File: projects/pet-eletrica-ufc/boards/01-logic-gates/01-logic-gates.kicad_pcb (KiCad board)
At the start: 2 copper layers, 114 x 144 mm, 18 parts, among them J1 5V INPUT, SW1 B3F-4050, SW2 B3F-4050, U1 SN74HC08N, U2 SN74HC32N, U3 SN74HC04N

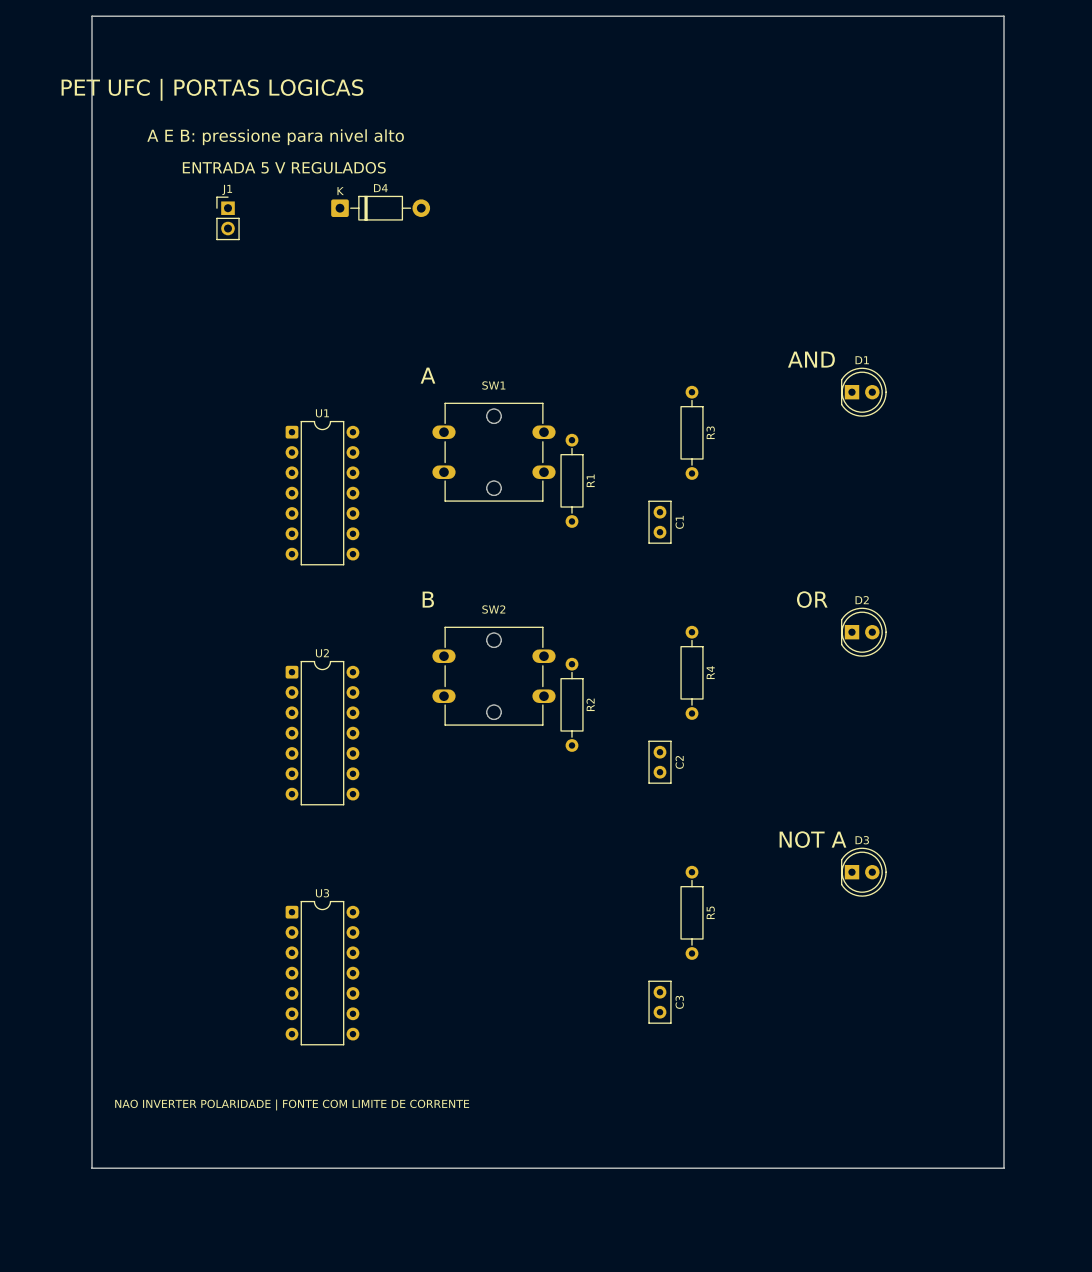
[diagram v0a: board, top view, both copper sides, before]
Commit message: feat(pet-ufc): implement discrete transistor logic board
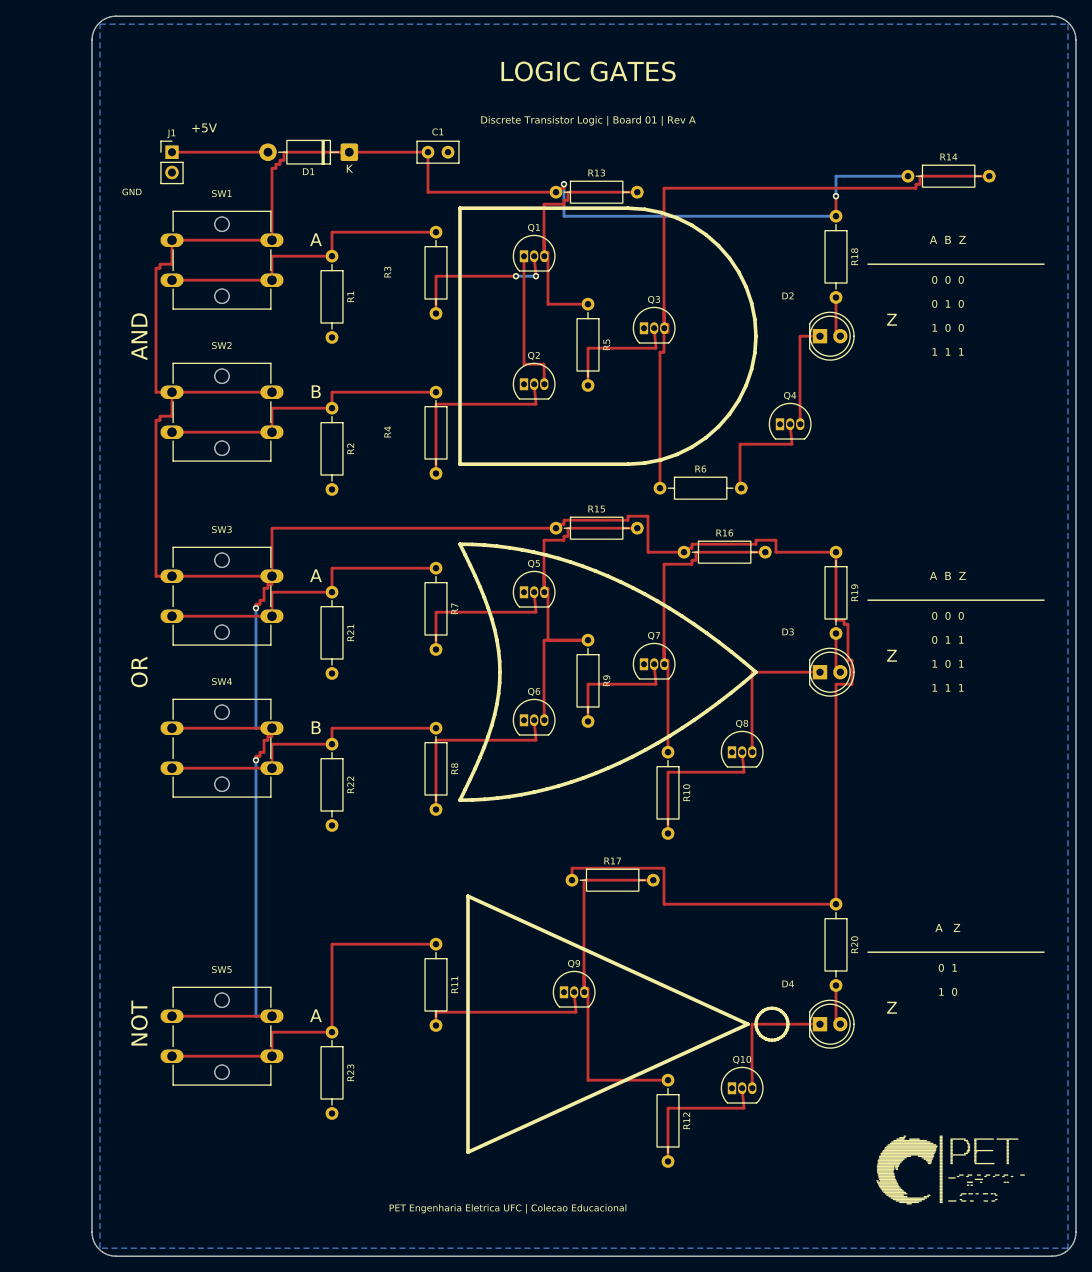
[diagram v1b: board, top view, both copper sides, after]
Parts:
- removed C2, C3: 100nF 50V, Capacitor_THT:C_Disc_D5.0mm_W2.5mm_P2.50mm
- removed U1: SN74HC08N, Package_DIP:DIP-14_W7.62mm
- removed U2: SN74HC32N, Package_DIP:DIP-14_W7.62mm
- removed U3: SN74HC04N, Package_DIP:DIP-14_W7.62mm
- added Q1: 2N3904, Package_TO_SOT_THT:TO-92_Inline, F.Cu at (57.0, 33.0)
- added Q10: 2N3904, Package_TO_SOT_THT:TO-92_Inline, F.Cu at (83.0, 137.0)
- added Q2: 2N3904, Package_TO_SOT_THT:TO-92_Inline, F.Cu at (57.0, 49.0)
- added Q3: 2N3904, Package_TO_SOT_THT:TO-92_Inline, F.Cu at (72.0, 42.0)
- added Q4: 2N3904, Package_TO_SOT_THT:TO-92_Inline, F.Cu at (89.0, 54.0)
- added Q5: 2N3904, Package_TO_SOT_THT:TO-92_Inline, F.Cu at (57.0, 75.0)
- added Q6: 2N3904, Package_TO_SOT_THT:TO-92_Inline, F.Cu at (57.0, 91.0)
- added Q7: 2N3904, Package_TO_SOT_THT:TO-92_Inline, F.Cu at (72.0, 84.0)
- added Q8: 2N3904, Package_TO_SOT_THT:TO-92_Inline, F.Cu at (83.0, 95.0)
- added Q9: 2N3904, Package_TO_SOT_THT:TO-92_Inline, F.Cu at (62.0, 125.0)
- added R10: 10k 5%, Resistor_THT:R_Axial_DIN0207_L6.3mm_D2.5mm_P10.16mm_Horizontal, F.Cu at (75.0, 95.0)
- added R11: 10k 5%, Resistor_THT:R_Axial_DIN0207_L6.3mm_D2.5mm_P10.16mm_Horizontal, F.Cu at (46.0, 119.0)
- added R12: 10k 5%, Resistor_THT:R_Axial_DIN0207_L6.3mm_D2.5mm_P10.16mm_Horizontal, F.Cu at (75.0, 136.0)
- added R13: 2.2k 5%, Resistor_THT:R_Axial_DIN0207_L6.3mm_D2.5mm_P10.16mm_Horizontal, F.Cu at (61.0, 25.0)
- added R14: 2.2k 5%, Resistor_THT:R_Axial_DIN0207_L6.3mm_D2.5mm_P10.16mm_Horizontal, F.Cu at (105.0, 23.0)
- added R15: 2.2k 5%, Resistor_THT:R_Axial_DIN0207_L6.3mm_D2.5mm_P10.16mm_Horizontal, F.Cu at (61.0, 67.0)
- added R16: 2.2k 5%, Resistor_THT:R_Axial_DIN0207_L6.3mm_D2.5mm_P10.16mm_Horizontal, F.Cu at (77.0, 70.0)
- added R17: 2.2k 5%, Resistor_THT:R_Axial_DIN0207_L6.3mm_D2.5mm_P10.16mm_Horizontal, F.Cu at (63.0, 111.0)
- added R18: 1.5k 5%, Resistor_THT:R_Axial_DIN0207_L6.3mm_D2.5mm_P10.16mm_Horizontal, F.Cu at (96.0, 28.0)
- added R19: 1.5k 5%, Resistor_THT:R_Axial_DIN0207_L6.3mm_D2.5mm_P10.16mm_Horizontal, F.Cu at (96.0, 70.0)
- added R20: 1.5k 5%, Resistor_THT:R_Axial_DIN0207_L6.3mm_D2.5mm_P10.16mm_Horizontal, F.Cu at (96.0, 114.0)
- added R21: 10k 5%, Resistor_THT:R_Axial_DIN0207_L6.3mm_D2.5mm_P10.16mm_Horizontal, F.Cu at (33.0, 75.0)
- added R22: 10k 5%, Resistor_THT:R_Axial_DIN0207_L6.3mm_D2.5mm_P10.16mm_Horizontal, F.Cu at (33.0, 94.0)
- added R23: 10k 5%, Resistor_THT:R_Axial_DIN0207_L6.3mm_D2.5mm_P10.16mm_Horizontal, F.Cu at (33.0, 130.0)
- added R6: 10k 5%, Resistor_THT:R_Axial_DIN0207_L6.3mm_D2.5mm_P10.16mm_Horizontal, F.Cu at (74.0, 62.0)
- added R7: 10k 5%, Resistor_THT:R_Axial_DIN0207_L6.3mm_D2.5mm_P10.16mm_Horizontal, F.Cu at (46.0, 72.0)
- added R8: 10k 5%, Resistor_THT:R_Axial_DIN0207_L6.3mm_D2.5mm_P10.16mm_Horizontal, F.Cu at (46.0, 92.0)
- added R9: 10k 5%, Resistor_THT:R_Axial_DIN0207_L6.3mm_D2.5mm_P10.16mm_Horizontal, F.Cu at (65.0, 81.0)
- added SW3: B3F-4050, Button_Switch_THT:SW_SPST_Omron_B3F-50xx, F.Cu at (13.0, 73.0)
- added SW4: B3F-4050, Button_Switch_THT:SW_SPST_Omron_B3F-50xx, F.Cu at (13.0, 92.0)
- added SW5: B3F-4050, Button_Switch_THT:SW_SPST_Omron_B3F-50xx, F.Cu at (13.0, 128.0)
- D1: value TLHR5200 -> 1N5819; footprint LED_THT:LED_D5.0mm -> Diode_THT:D_DO-41_SOD81_P10.16mm_Horizontal
- D4: value 1N5819 -> TLHR5200; footprint Diode_THT:D_DO-41_SOD81_P10.16mm_Horizontal -> LED_THT:LED_D5.0mm
- R3, R4, R5: value 1.5k 5% -> 10k 5%
- moved D4 118.3 mm to (94.0, 129.0)
- moved R5 72.2 mm to (65.0, 39.0)
- moved D1 69.6 mm to (35.2, 20.0), turned to 180 degrees
- moved C1 53.5 mm to (45.0, 20.0), turned to 0 degrees
- moved SW2 47.4 mm to (13.0, 50.0)
- moved R2 43.9 mm to (33.0, 52.0)
- moved R4 43.9 mm to (46.0, 50.0)
- moved SW1 41.6 mm to (13.0, 31.0)
- moved R1 37.8 mm to (33.0, 33.0)
- moved R3 37.7 mm to (46.0, 30.0)
- moved D2 37.2 mm to (94.0, 43.0)
- moved D3 25.3 mm to (94.0, 85.0)
- moved J1 9.90 mm to (13.0, 20.0)
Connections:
- C1 pad 1: VCC -> /VCC
- C1 pad 2: GND -> /GND
- D1 pad 1: GND -> /VCC
- D1 pad 2: LED1_A -> /5V_IN
- D2 pad 1: GND -> /LED_AND_K
- D2 pad 2: LED2_A -> /LED_AND_A
- D3 pad 1: GND -> /LED_OR_K
- D3 pad 2: LED3_A -> /LED_OR_A
- D4 pad 1: VCC -> /LED_NOT_K
- D4 pad 2: 5V_IN -> /LED_NOT_A
- J1 pad 1: 5V_IN -> /5V_IN
- J1 pad 2: GND -> /GND
- R1 pad 1: A -> /A_AND
- R1 pad 2: GND -> /GND
- R2 pad 1: B -> /B_AND
- R2 pad 2: GND -> /GND
- R3 pad 1: Y_AND -> /A_AND
- R3 pad 2: LED1_A -> /Q1_B
- R4 pad 1: Y_OR -> /B_AND
- R4 pad 2: LED2_A -> /Q2_B
- R5 pad 1: Y_NOT -> /N_AND
- R5 pad 2: LED3_A -> /Q3_B
- SW1 pad 1: VCC -> /VCC
- SW1 pad 2: A -> /A_AND
- SW2 pad 1: VCC -> /VCC
- SW2 pad 2: B -> /B_AND
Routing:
- net /VCC: track 0.00 -> 453.5 mm, vias 0 -> 4
- net /Y_AND: track 0.00 -> 83.5 mm
- net /N_OR: track 0.00 -> 49.0 mm
- net /A_NOT: track 0.00 -> 47.0 mm
- net /Y_NOT: track 0.00 -> 46.5 mm
- net /Y_OR: track 0.00 -> 40.5 mm
- net /A_OR: track 0.00 -> 39.0 mm
- net /A_AND: track 0.00 -> 39.0 mm
- net /B_OR: track 0.00 -> 38.0 mm
- net /B_AND: track 0.00 -> 38.0 mm
- net /N_AND: track 0.00 -> 33.5 mm
- net /Q6_B: track 0.00 -> 23.5 mm
- net /Q2_B: track 0.00 -> 23.5 mm
- net /Q9_B: track 0.00 -> 21.5 mm
- net /Q8_B: track 0.00 -> 19.5 mm
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- added copper zone on B.Cu, net /GND
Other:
- board size 114 x 144 mm -> 123 x 155 mm
- board text added: "+5V"
- board text added: "0 0 0"
- board text added: "0 1"
- board text added: "0 1 0"
- board text added: "0 1 1"
- board text added: "1 0"
- board text added: "1 0 0"
- board text added: "1 0 1"
- board text added: "1 1 1"
- board text added: "A B Z"
- board text added: "A Z"
- board text added: "Discrete Transistor Logic | Board 01 | Rev A"
- board text added: "GND"
- board text added: "LOGIC GATES"
- board text added: "NOT"
- board text added: "PET Engenharia Eletrica UFC | Colecao Educacional"
- board text added: "Z"
- board text removed: "A E B: pressione para nivel alto"
- board text removed: "ENTRADA 5 V REGULADOS"
- board text removed: "NAO INVERTER POLARIDADE | FONTE COM LIMITE DE CORRENTE"
- board text removed: "NOT A"
- board text removed: "PET UFC | PORTAS LOGICAS"
